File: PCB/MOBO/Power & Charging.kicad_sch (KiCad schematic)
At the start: 51 parts, among them J201 USB_C_Receptacle_PowerOnly_6P, Q1 PMOS, Q2 NMOS, Q3 NMOS, Q4 NMOS, Q5 PMOS, Q6 NMOS, Q7 DMP3013SFV, SW1 SW_DPST_x2, U1 BQ297xy, U2 AT90USB647-M, U202 MCP73871-1AA, U205 TPS61230DRC, U3 74LVC1G373

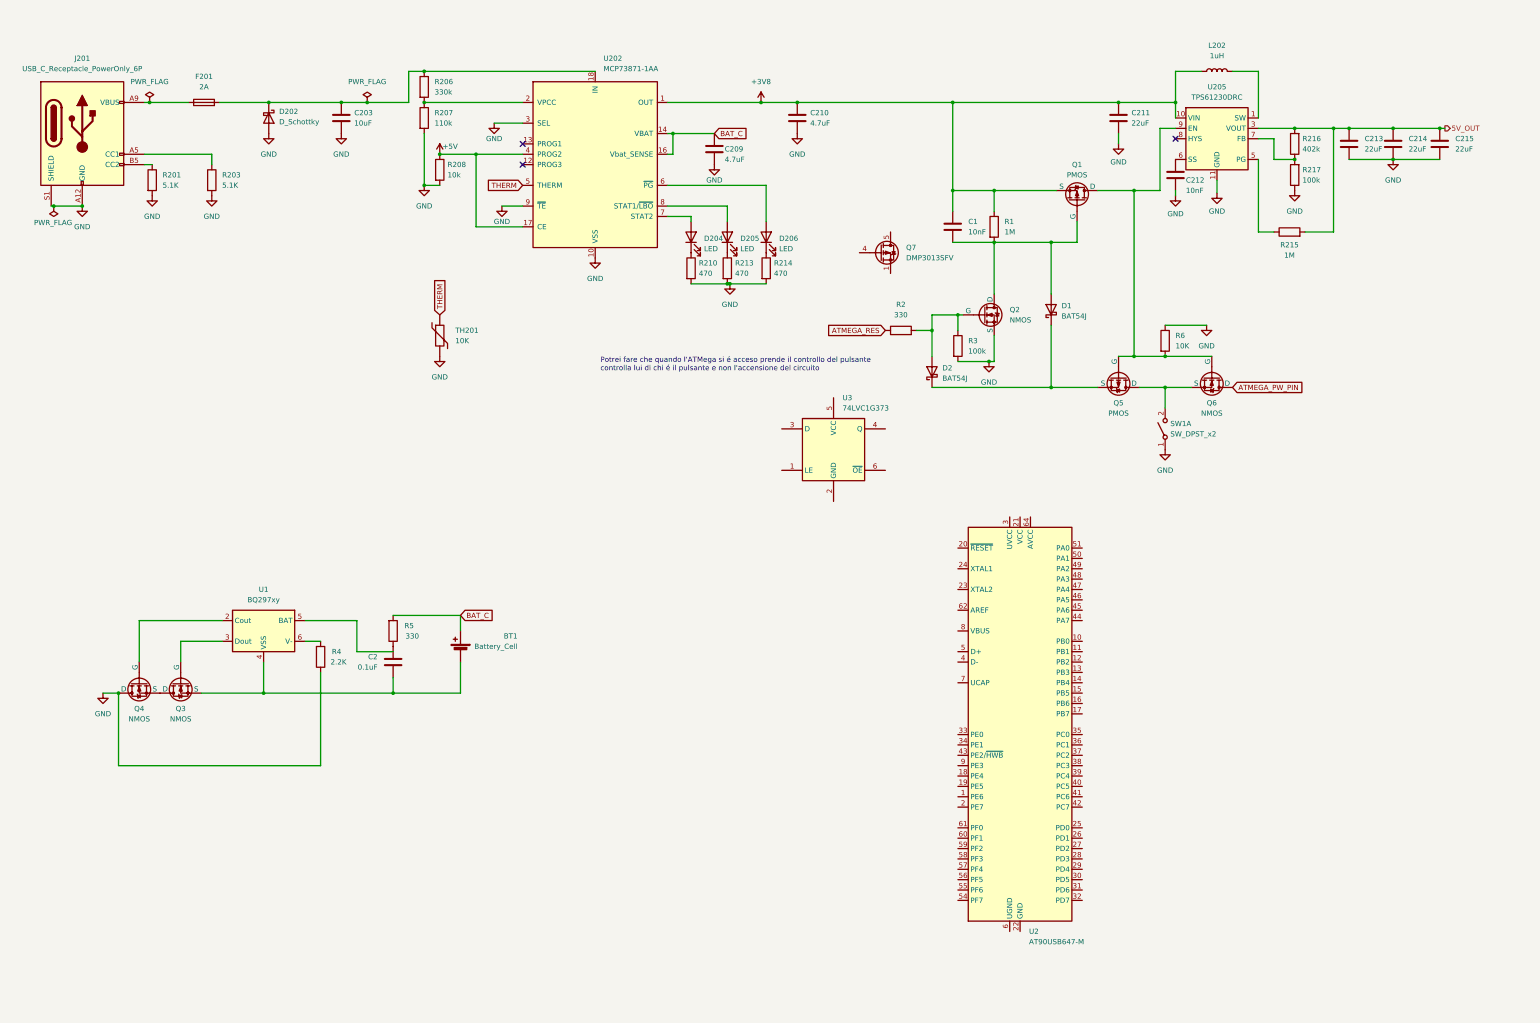
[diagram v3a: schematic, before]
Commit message: fixed latching circuit, missing mosfets dimensions
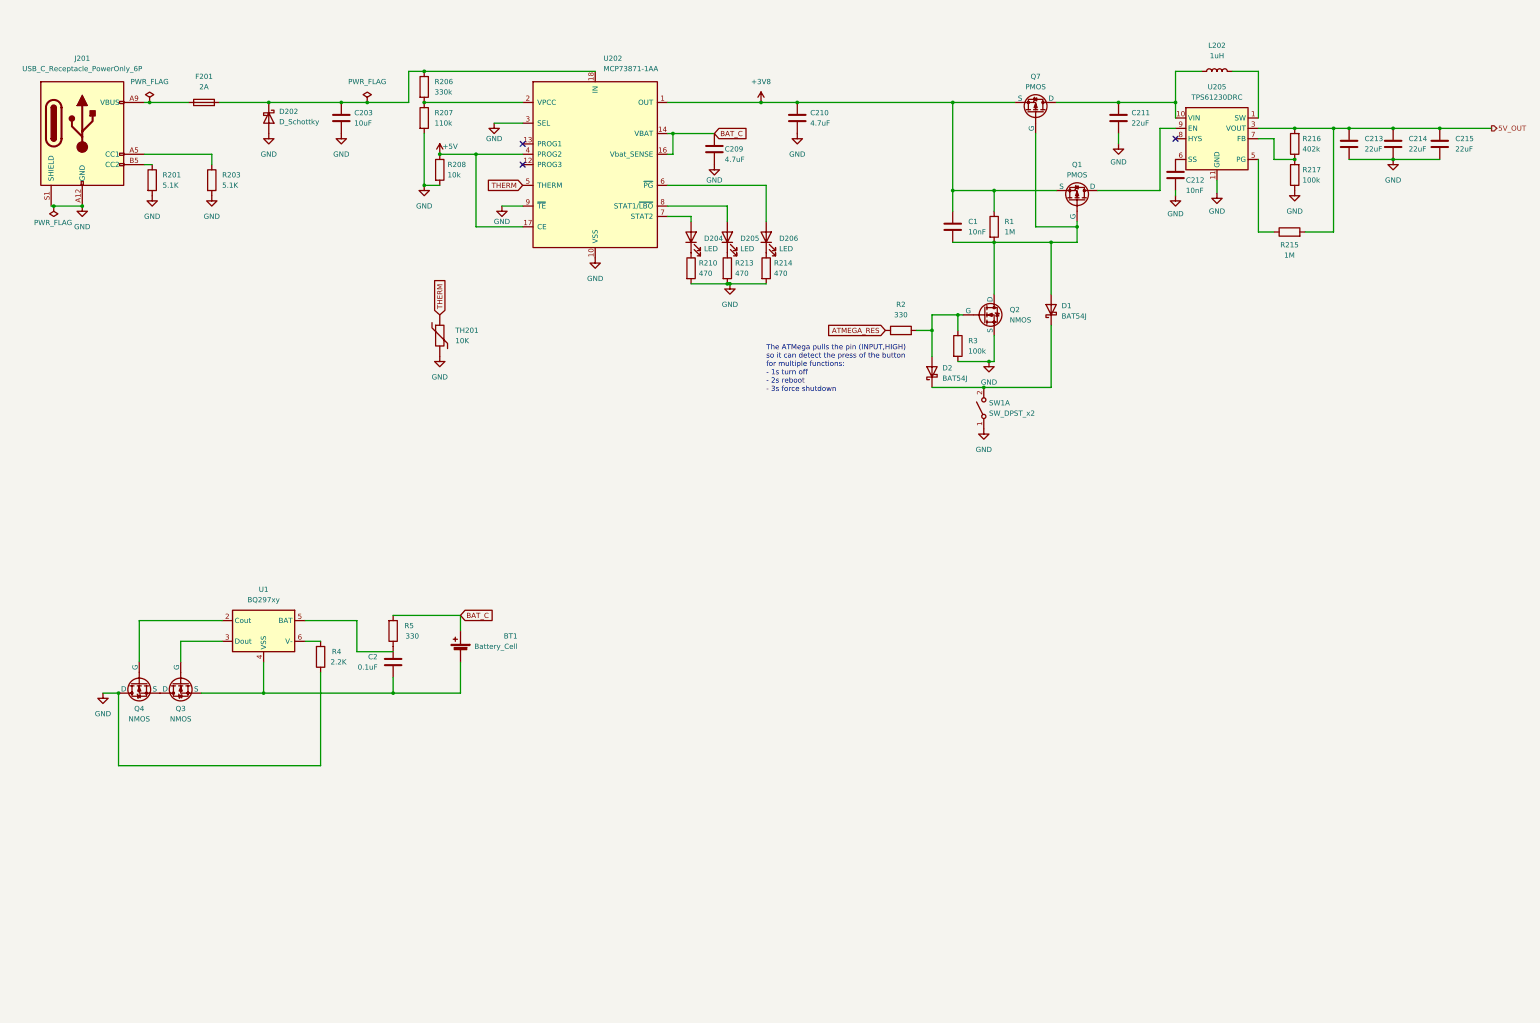
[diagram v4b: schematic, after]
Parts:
- removed Q5: PMOS, symbol Simulation_SPICE:PMOS
- removed Q6: NMOS, symbol Simulation_SPICE:NMOS
- removed Q7: DMP3013SFV, Package_SON:Diodes_PowerDI3333-8, symbol Transistor_FET:DMP3013SFV
- removed R6: 10K, symbol Device:R
- removed U2: AT90USB647-M, Package_DFN_QFN:QFN-64-1EP_9x9mm_P0.5mm_EP7.5x7.5mm, symbol MCU_Microchip_AVR:AT90USB647-M
- removed U3: 74LVC1G373, symbol 74xGxx:74LVC1G373
- added Q7: PMOS, symbol Simulation_SPICE:PMOS
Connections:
- net +3V8: now also Q7.3 (S); no longer C211.1, L202.1, U205.10 (VIN)
- net at SW1.2 (B): now also D1.1 (K), D2.1 (K)
- net at C1.2, D1.2 (A), Q1.2 (G)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: now also Q7.2 (G)
- new net: C211.1, L202.1, Q7.1 (D), U205.10 (VIN)
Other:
- note added: "The ATMega pulls the pin (INPUT,HIGH) so it can detect the press of the button for multiple functions: - 1s turn off - 2s reboot - 3s force shutdown"
- note removed: "Potrei fare che quando l'ATMega si é acceso prende il controllo del pulsante controlla lui di chi é il pulsante e non l'accensione del circuito"
- moved on the sheet: SW1A

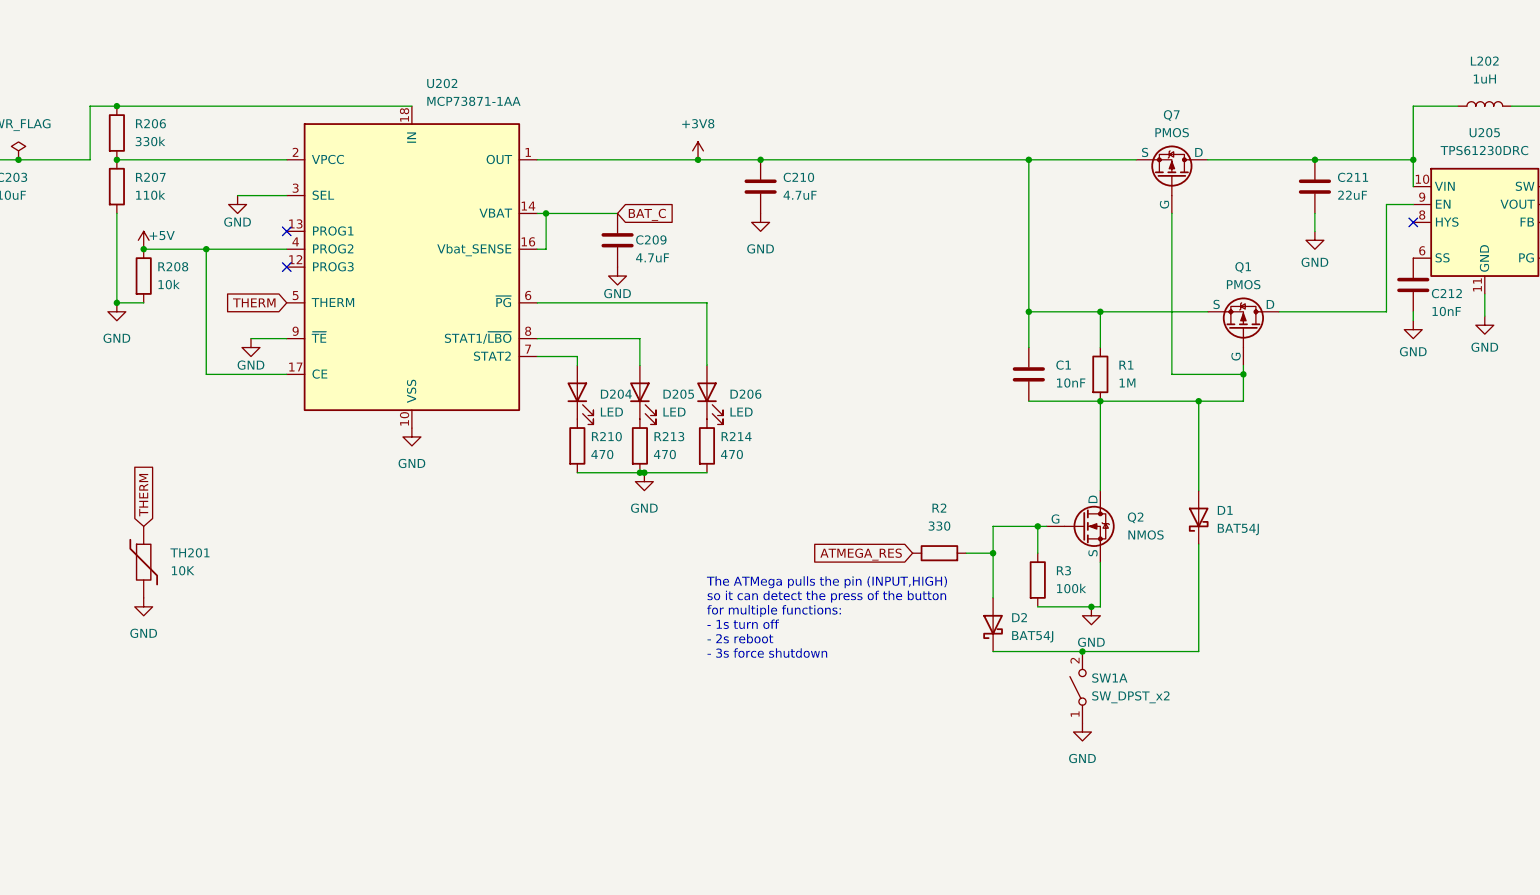
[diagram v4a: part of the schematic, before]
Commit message: Added mosfet dimensions
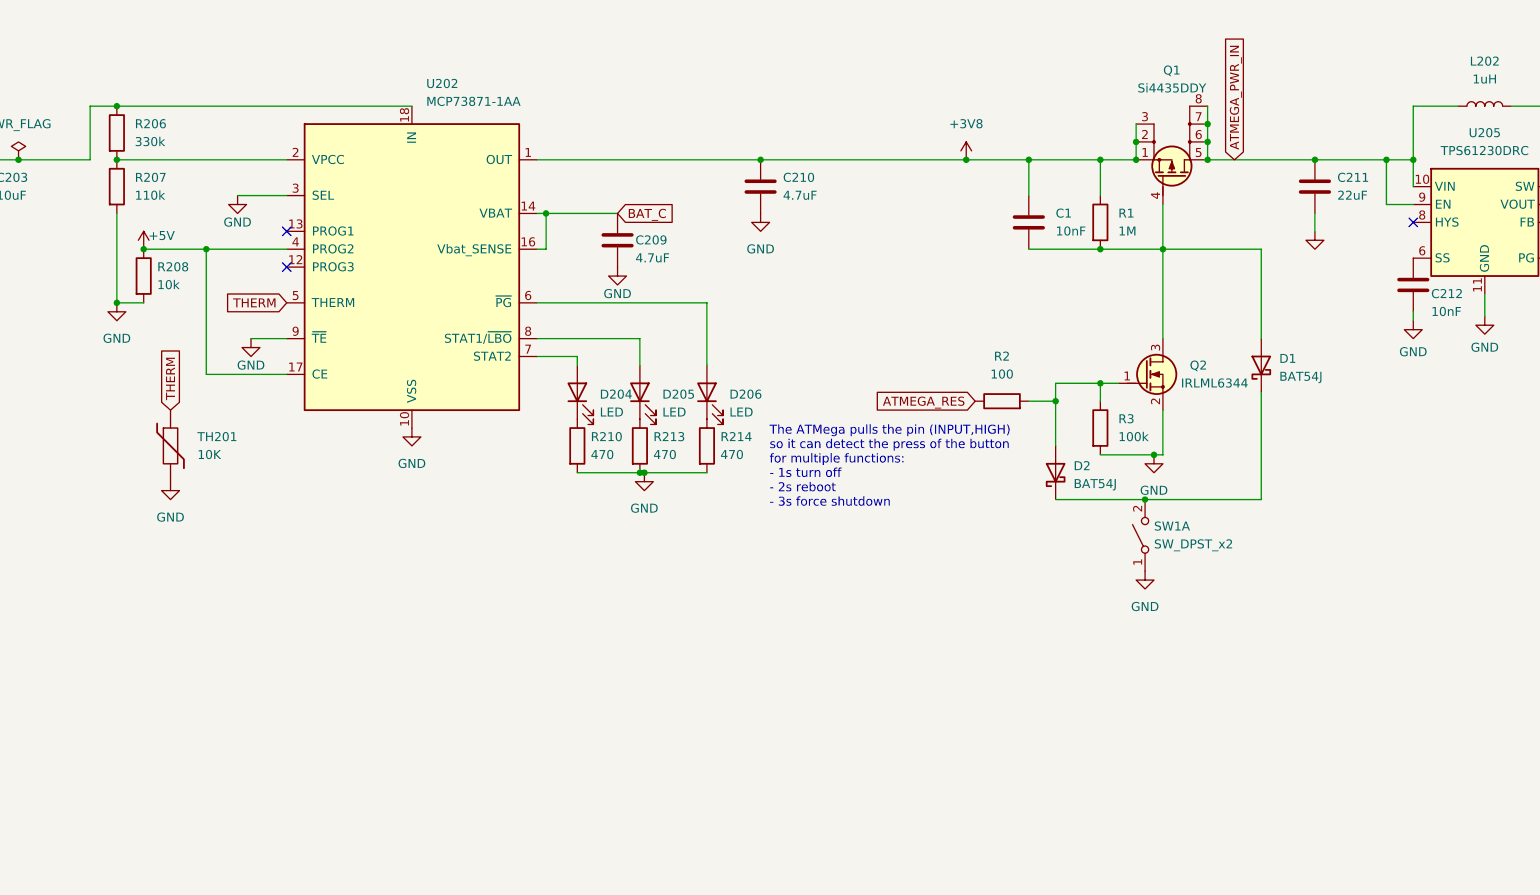
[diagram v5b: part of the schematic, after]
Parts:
- removed Q1, Q7: PMOS, symbol Simulation_SPICE:PMOS
- removed Q2: NMOS, symbol Simulation_SPICE:NMOS
- added Q1: Si4435DDY, Package_SO_AKL:SO-8_3.9x4.9mm_P1.27mm, symbol PCM_Transistor_MOSFET_AKL:Si4435DDY
- added Q2: IRLML6344, Package_TO_SOT_SMD_AKL:SOT-23, symbol PCM_Transistor_MOSFET_AKL:IRLML6344
- R2: value 330 -> 100
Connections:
- net +3V8: now also Q1.1 (S), Q1.2 (S), Q1.3 (S)
- net GND: now also Q2.2 (S)
- net at D2.2 (A), R2.2, R3.1: now also Q2.1 (G)
- net ATMEGA_PWR_IN: now reaches C211.1, L202.1, U205.10 (VIN)
- net ATMEGA_PWR_IN: now also U205.9 (EN), Q1.5 (D), Q1.6 (D), Q1.7 (D), Q1.8 (D)
- net at C1.2, D1.2 (A), R1.2: now also Q1.4 (G), Q2.3 (D)
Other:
- moved on the sheet: C1, D1, D2, R1, R2, R3, SW1A, TH201

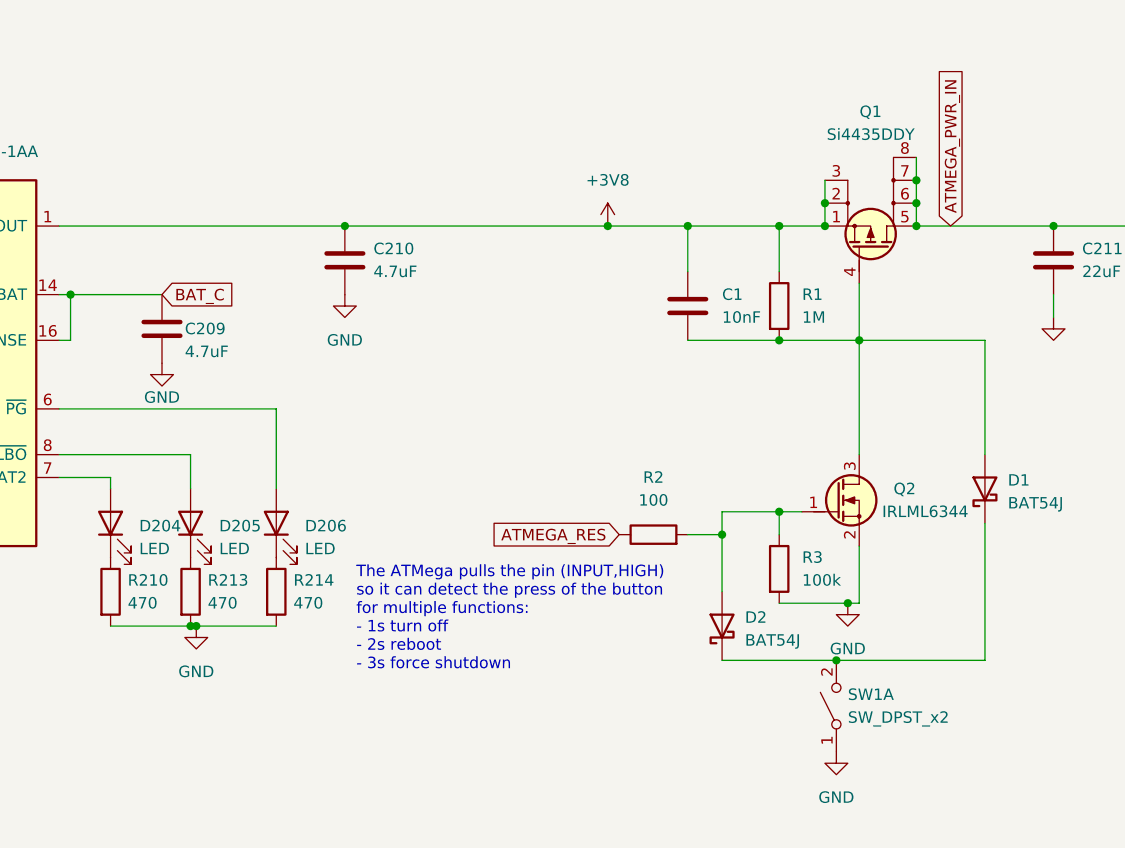
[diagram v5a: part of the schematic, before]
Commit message: added MOSFETs
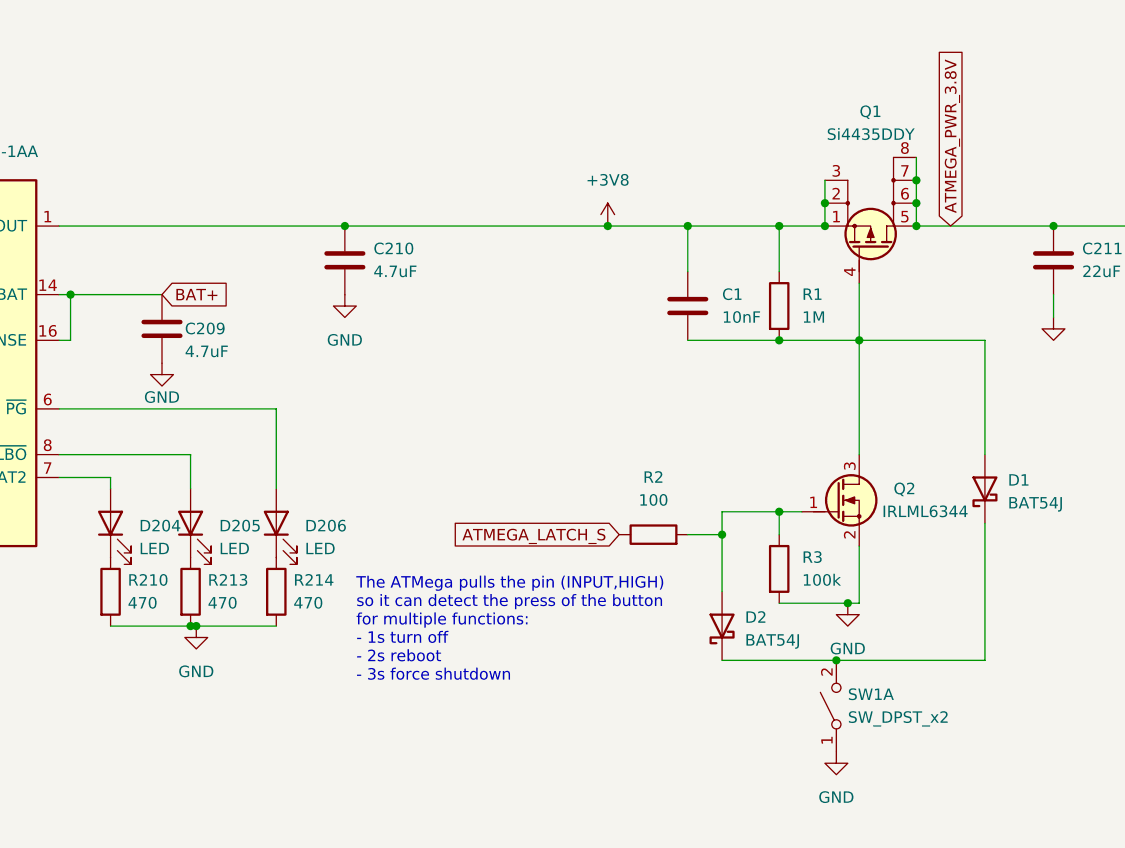
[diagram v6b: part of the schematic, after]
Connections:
- net BAT_C: no longer C209.1, U202.14 (VBAT), U202.15 (VBAT), U202.16 (Vbat_SENSE)
- net ATMEGA_PWR_IN renamed ATMEGA_PWR_3.8V
- net ATMEGA_RES renamed ATMEGA_LATCH_S
- new net BAT+: C209.1, U202.14 (VBAT), U202.15 (VBAT), U202.16 (Vbat_SENSE)
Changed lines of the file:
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@@
   )
   (text "The ATMega pulls the pin (INPUT,HIGH) \nso it can detect the press of the button\nfor multiple functions:\n- 1s turn off\n- 2s reboot\n- 3s force shutdown\n"
-    (at 205.74 86.36 0)
+    (at 205.74 87.63 0)
     (effects (font (size 1.27 1.27)) (justify left bottom))
   )
-  (global_label "BAT_C" (shape input) (at 184.15 44.45 0) (fields_autoplaced)
+  (global_label "BAT+" (shape input) (at 184.15 44.45 0) (fields_autoplaced)
     (effects (font (size 1.27 1.27)) (justify left))
-    (property "Intersheetrefs" "${INTERSHEET_REFS}" (at 192.699 44.45 0)
+    (property "Intersheetrefs" "${INTERSHEET_REFS}" (at 192.0338 44.45 0)
       (effects (font (size 1.27 1.27)) (justify left) hide)
     )
   )
-  (global_label "ATMEGA_PWR_IN" (shape input) (at 271.78 36.83 90) (fields_autoplaced)
+  (global_label "ATMEGA_PWR_3.8V" (shape input) (at 271.78 36.83 90) (fields_autoplaced)
     (effects (font (size 1.27 1.27)) (justify left))
-    (property "Intersheetrefs" "${INTERSHEET_REFS}" (at 271.78 18.9677 90)
+    (property "Intersheetrefs" "${INTERSHEET_REFS}" (at 271.78 16.7906 90)
       (effects (font (size 1.27 1.27)) (justify left) hide)
     )
@@
     )
   )
-  (global_label "ATMEGA_RES" (shape input) (at 234.95 71.12 180) (fields_autoplaced)
+  (global_label "ATMEGA_LATCH_S" (shape input) (at 234.95 71.12 180) (fields_autoplaced)
     (effects (font (size 1.27 1.27)) (justify right))
-    (property "Intersheetrefs" "${INTERSHEET_REFS}" (at 220.3535 71.12 0)
+    (property "Intersheetrefs" "${INTERSHEET_REFS}" (at 216.1201 71.12 0)
       (effects (font (size 1.27 1.27)) (justify right) hide)
     )
@@
   )
   (symbol (lib_id "Device:C") (at 105.41 173.99 0) (mirror y) (unit 1)
-    (in_bom yes) (on_board yes) (dnp no) (fields_autoplaced)
+    (in_bom yes) (on_board yes) (dnp no)
     (property "Reference" "C2" (at 101.6 172.72 0)
       (effects (font (size 1.27 1.27)) (justify left))
